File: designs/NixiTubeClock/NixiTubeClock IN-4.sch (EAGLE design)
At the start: 15 parts, among them IC1 74141N, IC2 74HCT595D, IC3 74141N, IC4 74141N, IC5 74HCT595D, IC6 74141N

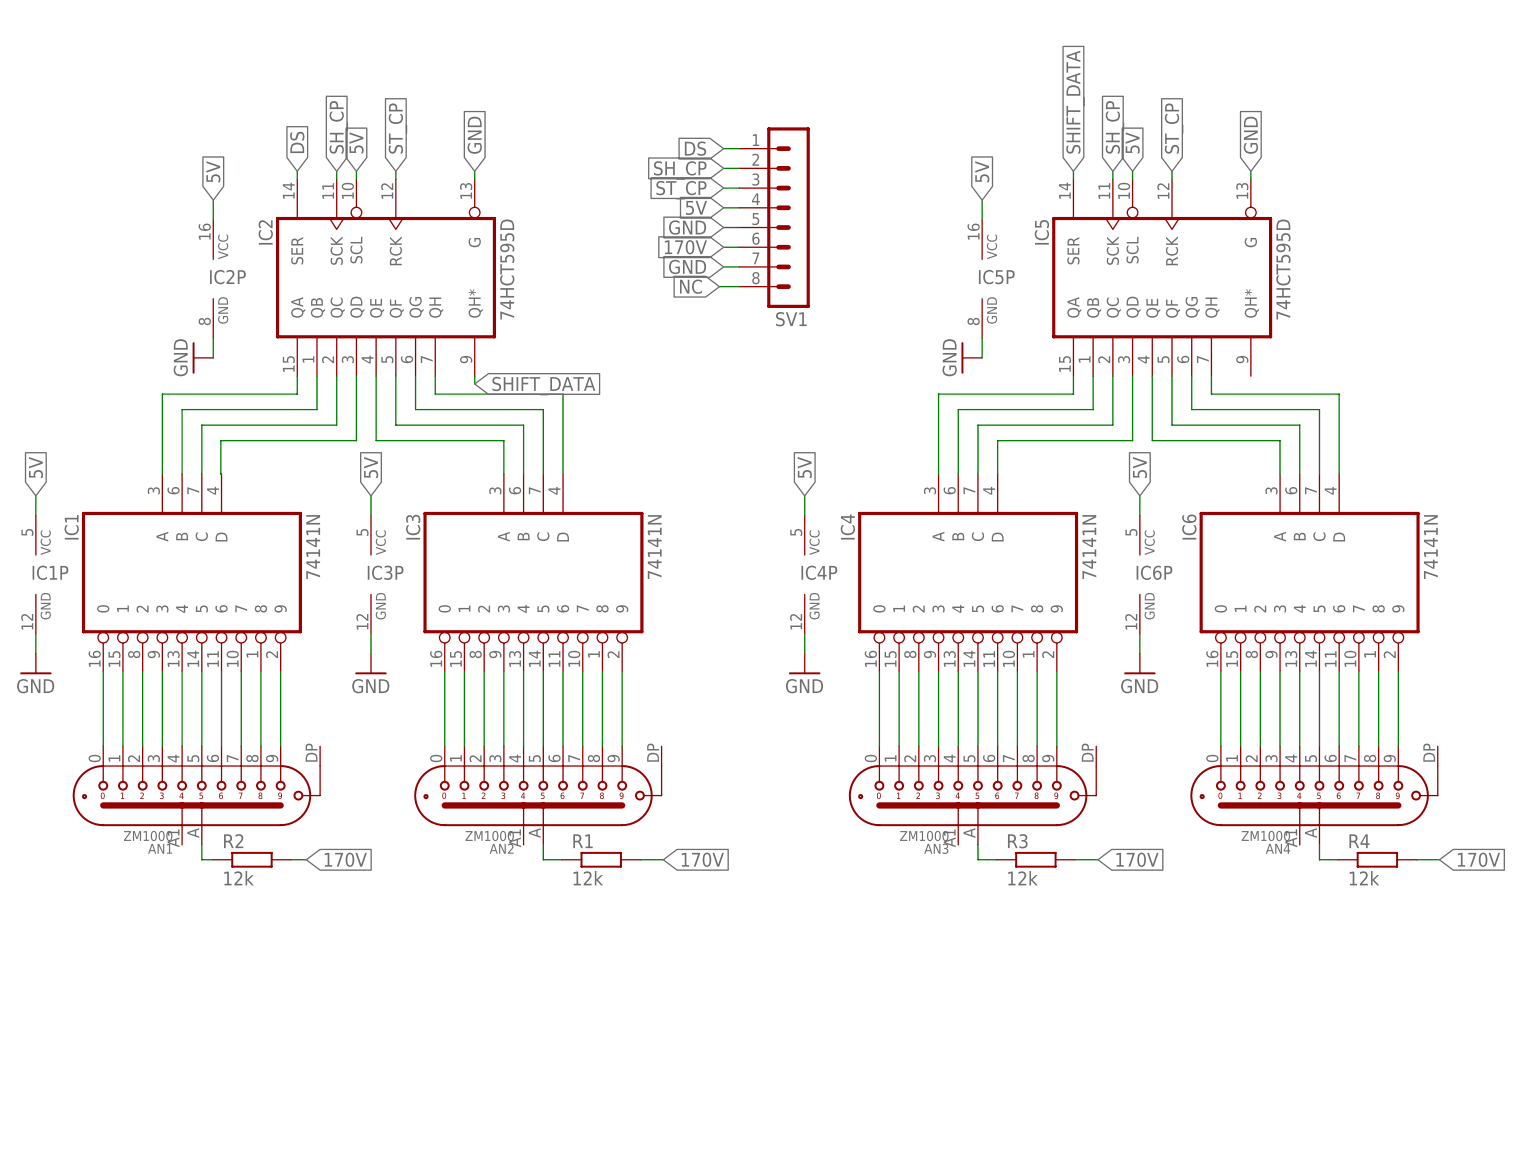
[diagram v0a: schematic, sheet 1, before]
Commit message: added first IN-4 Design and edited mainboard to fit all screws for IN-4
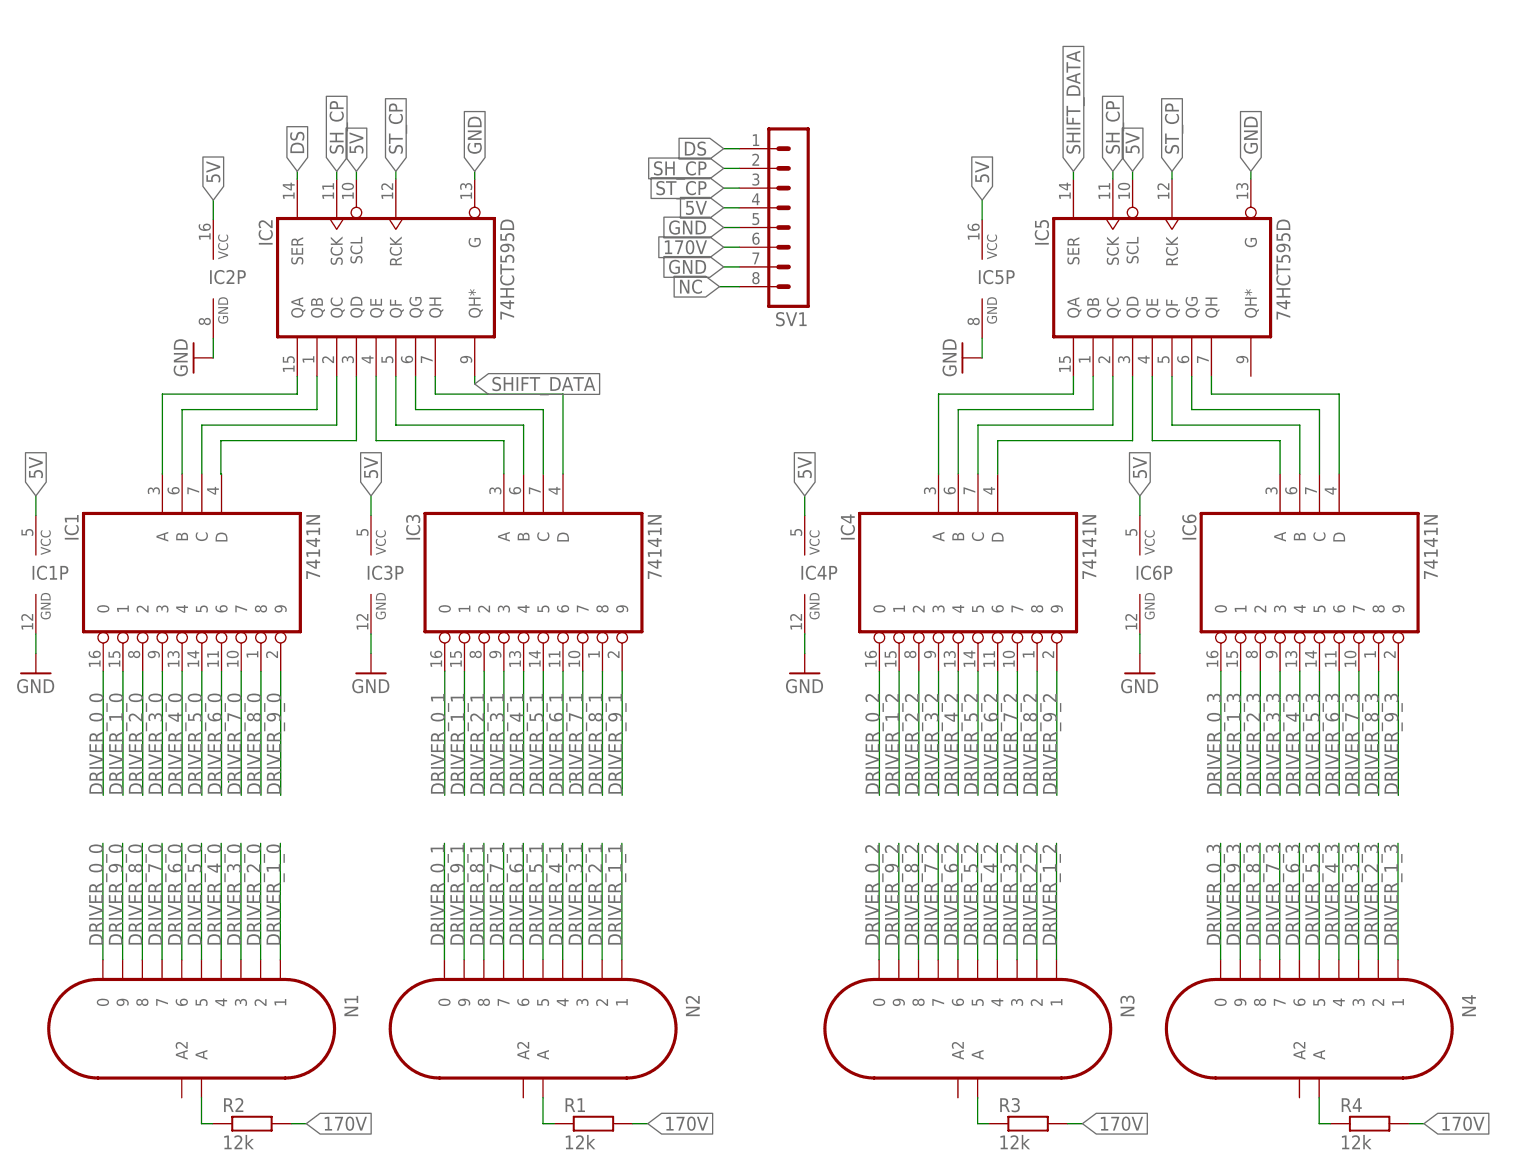
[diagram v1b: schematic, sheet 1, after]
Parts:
- removed AN1, AN2, AN3, AN4: ZM1000, NixieTube:ZM1000
- added N1, N2, N3, N4: IN-4, NixieTube:IN-4
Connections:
- removed net N$100: AN4.A1, R4.1
- removed net N$13: AN1.2, IC1A.2
- removed net N$15: AN1.3, IC1A.3
- removed net N$16: AN1.4, IC1A.4
- removed net N$17: AN1.5, IC1A.5
- removed net N$18: AN1.6, IC1A.6
- removed net N$19: AN1.7, IC1A.7
- removed net N$20: AN1.8, IC1A.8
- removed net N$21: AN1.9, IC1A.9
- removed net N$22: AN2.0, IC3A.0
- removed net N$23: AN2.1, IC3A.1
- removed net N$24: AN2.2, IC3A.2
- removed net N$25: AN2.3, IC3A.3
- removed net N$26: AN2.4, IC3A.4
- removed net N$27: AN2.5, IC3A.5
- removed net N$28: AN2.6, IC3A.6
- removed net N$29: AN2.7, IC3A.7
- removed net N$30: AN2.8, IC3A.8
- removed net N$31: AN2.9, IC3A.9
- removed net N$32: AN3.0, IC4A.0
- removed net N$35: AN3.1, IC4A.1
- removed net N$36: AN3.2, IC4A.2
- removed net N$66: AN3.3, IC4A.3
- removed net N$67: AN3.4, IC4A.4
- removed net N$68: AN3.5, IC4A.5
- removed net N$69: AN3.6, IC4A.6
- removed net N$70: AN3.7, IC4A.7
- removed net N$71: AN3.8, IC4A.8
- removed net N$72: AN3.9, IC4A.9
- removed net N$73: AN4.0, IC6A.0
- removed net N$74: AN4.1, IC6A.1
- removed net N$75: AN4.2, IC6A.2
- removed net N$76: AN4.3, IC6A.3
- removed net N$9: AN1.1, IC1A.1
- removed net N$91: AN4.4, IC6A.4
- removed net N$92: AN4.5, IC6A.5
- removed net N$93: AN4.6, IC6A.6
- removed net N$94: AN4.7, IC6A.7
- removed net N$95: AN4.8, IC6A.8
- removed net N$96: AN4.9, IC6A.9
- removed net N$97: AN1.A1, R2.1
- removed net N$98: AN2.A1, R1.1
- removed net N$99: AN3.A1, R3.1
- new net DRIVER_0_0: IC1A.0, N1.0
- new net DRIVER_0_1: IC3A.0, N2.0
- new net DRIVER_0_2: IC4A.0, N3.0
- new net DRIVER_0_3: IC6A.0, N4.0
- new net DRIVER_1_0: IC1A.1, N1.1
- new net DRIVER_1_1: IC3A.1, N2.1
- new net DRIVER_1_2: IC4A.1, N3.1
- new net DRIVER_1_3: IC6A.1, N4.1
- new net DRIVER_2_0: IC1A.2, N1.2
- new net DRIVER_2_1: IC3A.2, N2.2
- new net DRIVER_2_2: IC4A.2, N3.2
- new net DRIVER_2_3: IC6A.2, N4.2
- new net DRIVER_3_0: IC1A.3, N1.3
- new net DRIVER_3_1: IC3A.3, N2.3
- new net DRIVER_3_2: IC4A.3, N3.3
- new net DRIVER_3_3: IC6A.3, N4.3
- new net DRIVER_4_0: IC1A.4, N1.4
- new net DRIVER_4_1: IC3A.4, N2.4
- new net DRIVER_4_2: IC4A.4, N3.4
- new net DRIVER_4_3: IC6A.4, N4.4
- new net DRIVER_5_0: IC1A.5, N1.5
- new net DRIVER_5_1: IC3A.5, N2.5
- new net DRIVER_5_2: IC4A.5, N3.5
- new net DRIVER_5_3: IC6A.5, N4.5
- new net DRIVER_6_0: IC1A.6, N1.6
- new net DRIVER_6_1: IC3A.6, N2.6
- new net DRIVER_6_2: IC4A.6, N3.6
- new net DRIVER_6_3: IC6A.6, N4.6
- new net DRIVER_7_0: IC1A.7, N1.7
- new net DRIVER_7_1: IC3A.7, N2.7
- new net DRIVER_7_2: IC4A.7, N3.7
- new net DRIVER_7_3: IC6A.7, N4.7
- new net DRIVER_8_0: IC1A.8, N1.8
- new net DRIVER_8_1: IC3A.8, N2.8
- new net DRIVER_8_2: IC4A.8, N3.8
- new net DRIVER_8_3: IC6A.8, N4.8
- new net DRIVER_9_0: IC1A.9, N1.9
- new net DRIVER_9_1: IC3A.9, N2.9
- new net DRIVER_9_2: IC4A.9, N3.9
- new net DRIVER_9_3: IC6A.9, N4.9
- new net N$12: N1.A, R2.1
- new net N$4: N2.A, R1.1
- new net N$5: N3.A, R3.1
- net N$7: now also N4.A, R4.1; no longer AN1.0, IC1A.0
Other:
- moved on the sheet: R1, R2, R3, R4
